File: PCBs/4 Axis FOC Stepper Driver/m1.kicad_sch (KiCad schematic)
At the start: 16 parts, among them M1 Stepper_Motor_bipolar, U3 TSV994, U5 L298N

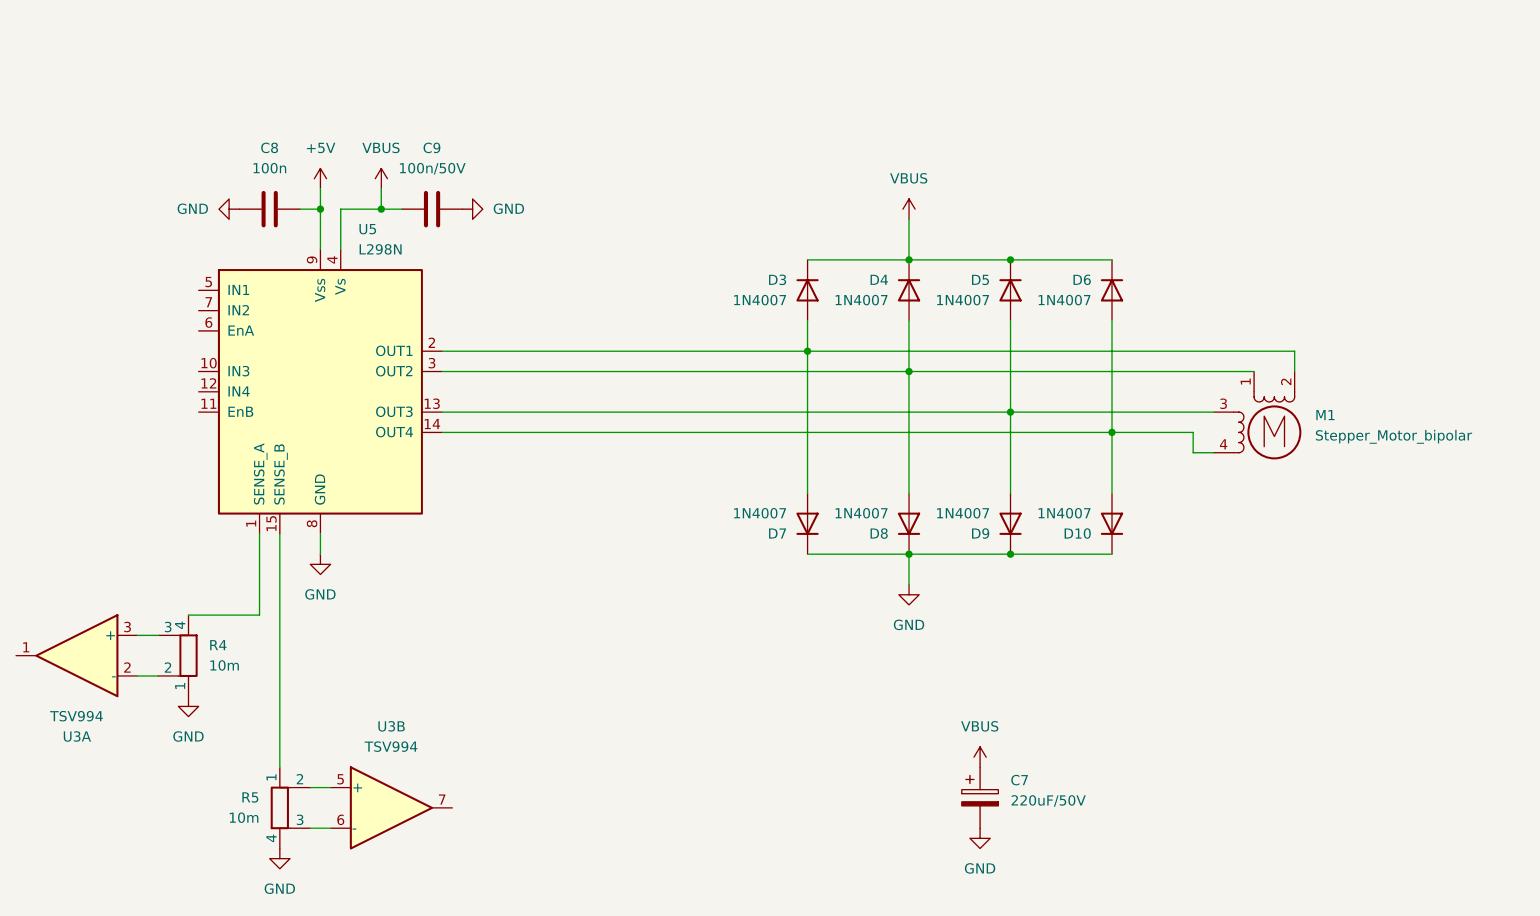
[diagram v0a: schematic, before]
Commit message: Hopefully finally chose a motor driver
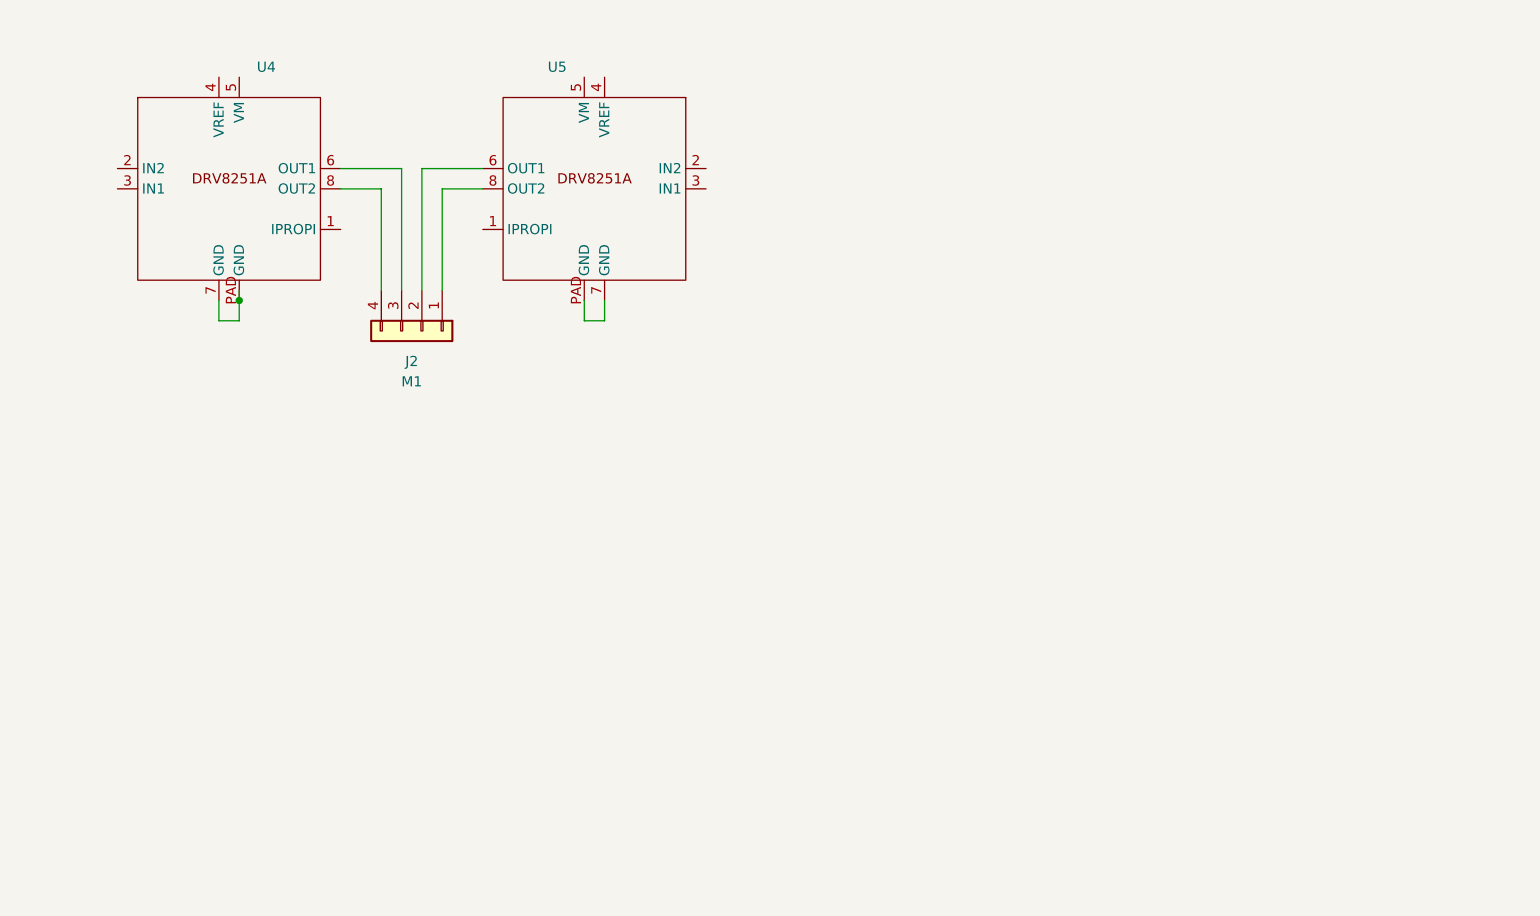
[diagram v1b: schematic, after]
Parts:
- removed C7: 220uF/50V, symbol Device:C_Polarized
- removed C8: 100n, symbol Device:C
- removed C9: 100n/50V, symbol Device:C
- removed D10, D3, D4, D5, D6, D7, D8, D9: 1N4007, symbol Device:D
- removed M1: Stepper_Motor_bipolar, symbol Motor:Stepper_Motor_bipolar
- removed R4, R5: 10m, Resistor_SMD:R_1206_3216Metric_Pad1.30x1.75mm_HandSolder, symbol Device:R_Shunt
- removed U3: TSV994, symbol Amplifier_Operational:TSV994
- removed U5: L298N, Package_TO_SOT_THT:TO-220-15_P2.54x2.54mm_StaggerOdd_Lead4.58mm_Vertical, symbol Driver_Motor:L298N
- added J2: M1, symbol Connector_Generic:Conn_01x04
- added U4, U5: ~, symbol EchoSymbols:DRV8251A
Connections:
- new net: J2.3 (Pin_3), U4.6 (OUT1)
- new net: U4.7 (GND), U4.PAD (GND)
- new net: J2.4 (Pin_4), U4.8 (OUT2)
- new net: J2.1 (Pin_1), U5.8 (OUT2)
- new net: J2.2 (Pin_2), U5.6 (OUT1)
- new net: U5.7 (GND), U5.PAD (GND)

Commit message: Start working on an integrated stepper driver
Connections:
- net M1B_I: now reaches U4.1 (IPROPI)
- net GND: now reaches U4.7 (GND), U4.PAD (GND)
- net GND: now also U5.7 (GND), U5.PAD (GND)
- net at J2.1 (Pin_1): now also U5.6 (OUT1); no longer U5.8 (OUT2)
- net at J2.2 (Pin_2): now also U5.8 (OUT2); no longer U5.6 (OUT1)
- net M1A_I: now reaches U5.1 (IPROPI)
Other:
- moved on the sheet: J2, U4
